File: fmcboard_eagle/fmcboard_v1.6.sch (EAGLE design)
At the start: 234 parts, among them IC1 OPA699ID, IC10 LM358, IC11 7805DT, IC12 SN74AUC2G66DCTR, IC13 SN74AUC2G66DCTR, IC14 SN74AUC2G66DCTR, IC15 SN74AUC2G66DCTR, IC16 DAC7578SPWR, IC17 SN74AUC2G66DCTR, IC18 SN74AUC2G66DCTR, IC19 SN74AUC2G66DCTR, IC2 DAC7578SPWR, IC20 SN74AUC2G66DCTR, IC21 74AUP2GU04GW, IC22 74AUP2GU04GW, IC23 74AUP2GU04GW, IC24 74AUP2GU04GW, IC25 MC7905ACD2TR4G, IC26 AMS1117-1.8, IC29 LM337KVURG3, IC3 LTC6229IMS8E#TRPBF, IC4 OPA695IDR, IC5 LTC6229IMS8E#TRPBF, IC6 OPA695IDR, IC7 OPA699ID, IC8 LM358, IC9 LM358, J1 8pin, J10 4p-2.54, J11 4p-2.54, J12 4p-2.54, J13 4p-2.54, J2 ASP-134604-01, J3 4p-2.54, J4 4p-2.54, J5 4p-2.54, J6 4p-2.54, J7 4p-2.54, J8 4p-2.54, J9 8pin, U1 TXS0108EPWR

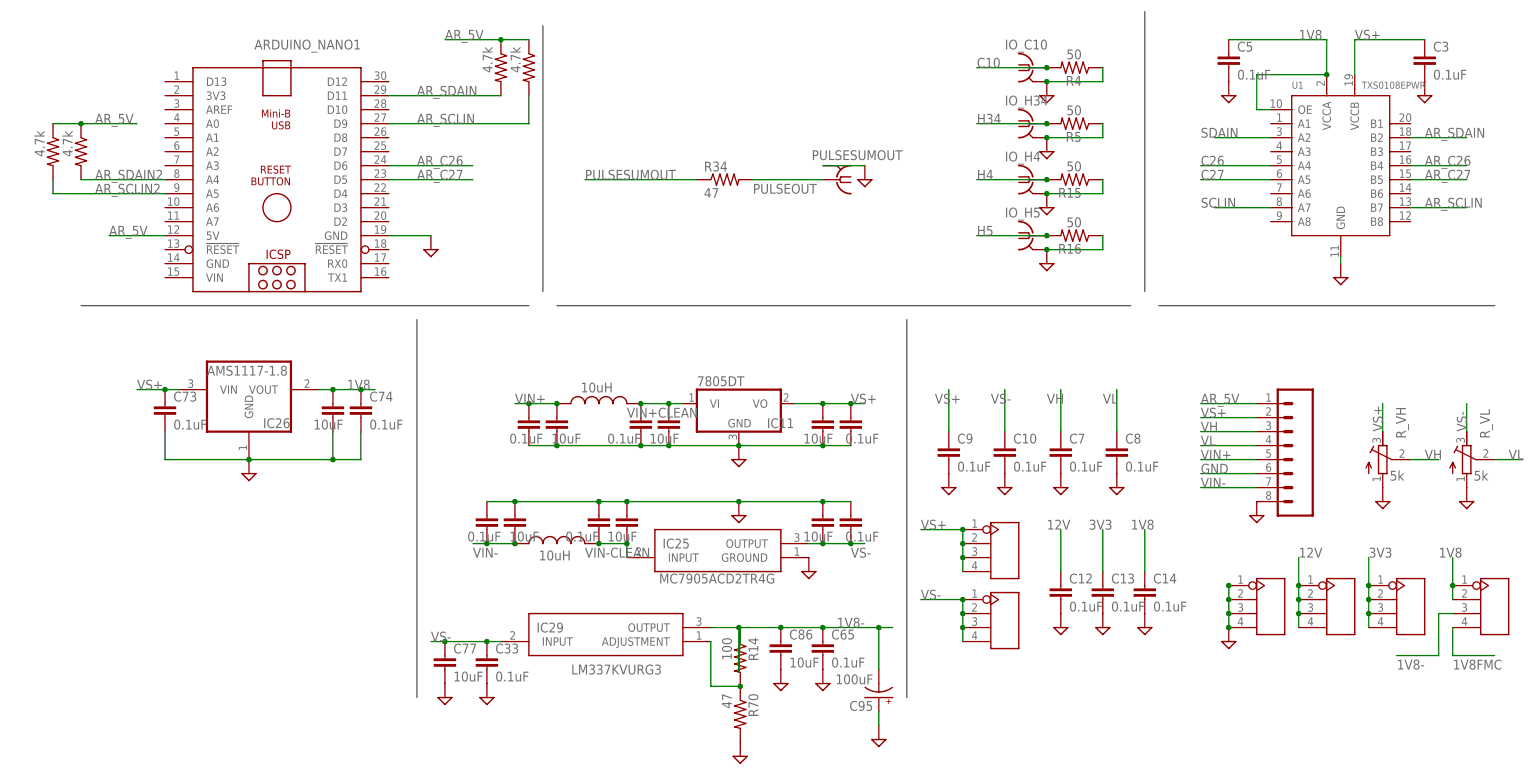
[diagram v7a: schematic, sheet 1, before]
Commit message: v1.65 C26 and C27 to A0 and A1 on arduino Remove level shifter, replace with 4.7k resistors
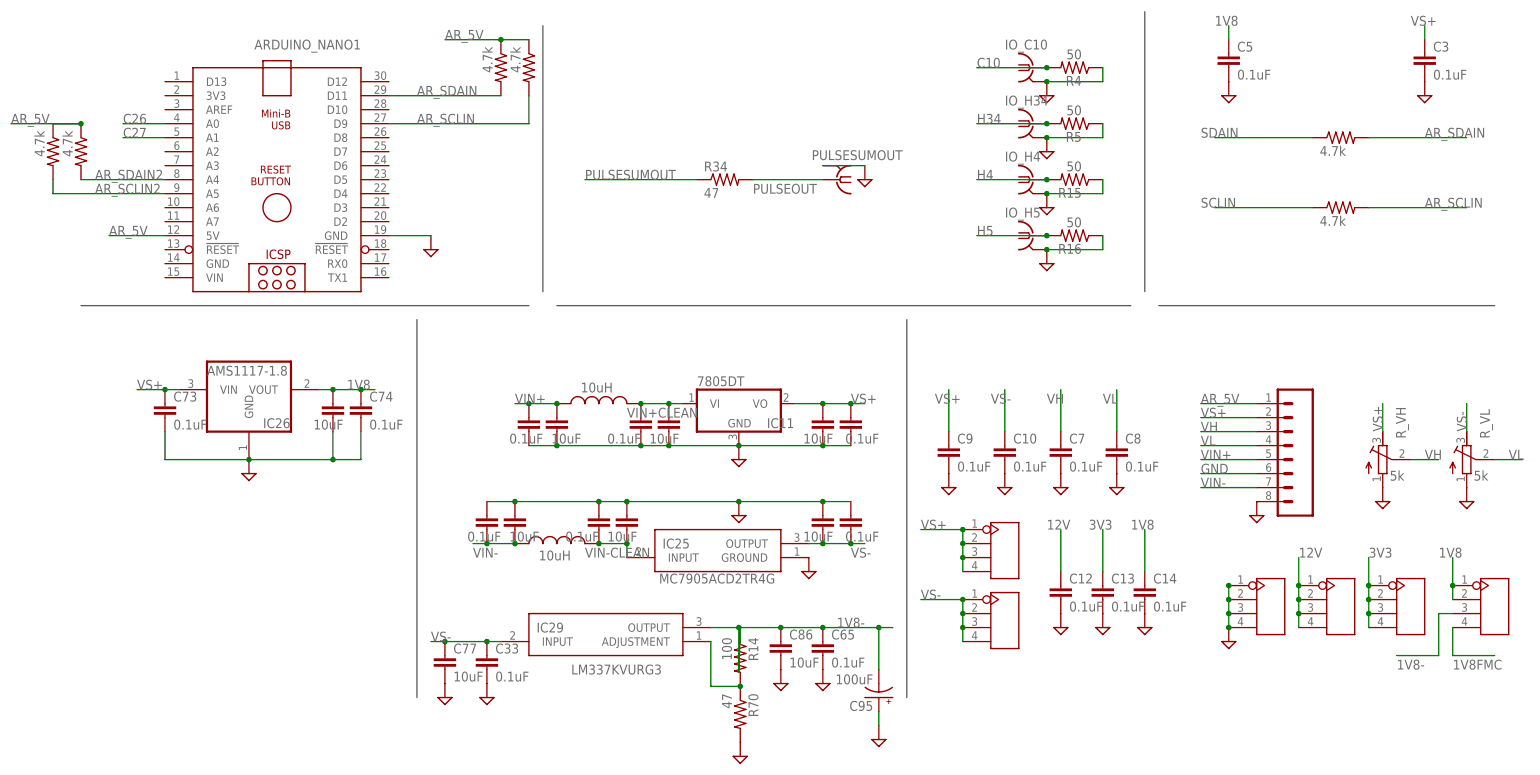
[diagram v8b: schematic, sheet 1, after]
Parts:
- removed U1: TXS0108EPWR, Seeed-IC:LOGIC-TXS0108EPWR(TSSOP20)
- added R87, R90: 4.7k, rcl:R-US_R0805
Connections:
- removed net AR_C26: ARDUINO_NANO1.D6, U1.B4
- removed net AR_C27: ARDUINO_NANO1.D5, U1.B5
- net 1V8: no longer U1.OE, U1.VCCA
- net AR_SCLIN: now also R90.2; no longer U1.B7
- net AR_SDAIN: now also R87.2; no longer U1.B2
- net C26: now also ARDUINO_NANO1.A0; no longer U1.A4
- net C27: now also ARDUINO_NANO1.A1; no longer U1.A5
- net GND: no longer U1.GND
- net SCLIN: now also R90.1; no longer U1.A7
- net SDAIN: now also R87.1; no longer U1.A2
- net VS+: no longer U1.VCCB
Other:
- note added: "Level limiter"
- note removed: "Level shifter"
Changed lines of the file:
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@@
 <part name="SUPPLY3" library="supply2" library_urn="urn:adsk.eagle:library:372" deviceset="GND" device=""/>
 <part name="SUPPLY7" library="supply2" library_urn="urn:adsk.eagle:library:372" deviceset="GND" device=""/>
-<part name="U1" library="Seeed-IC" library_urn="urn:adsk.eagle:library:470" deviceset="LOGIC-TXS0108EPWR(TSSOP20)" device="" package3d_urn="urn:adsk.eagle:package:32642/1" value="TXS0108EPWR"/>
-<part name="SUPPLY8" library="supply2" library_urn="urn:adsk.eagle:library:372" deviceset="GND" device=""/>
 <part name="C3" library="SparkFun-Passives" deviceset="CAP" device="0805" value="0.1uF"/>
 <part name="C5" library="SparkFun-Passives" deviceset="CAP" device="0805" value="0.1uF"/>
@@
 <part name="J10" library="Seeed-Connector" library_urn="urn:adsk.eagle:library:478" deviceset="DIP-BLACK-FEMALE-HEADER-VERT(4P-2.54)" device="" package3d_urn="urn:adsk.eagle:package:33137/1" value="4p-2.54"/>
 <part name="SUPPLY68" library="supply2" library_urn="urn:adsk.eagle:library:372" deviceset="GND" device=""/>
+<part name="R87" library="rcl" library_urn="urn:adsk.eagle:library:334" deviceset="R-US_" device="R0805" package3d_urn="urn:adsk.eagle:package:23553/2" value="4.7k"/>
+<part name="R90" library="rcl" library_urn="urn:adsk.eagle:library:334" deviceset="R-US_" device="R0805" package3d_urn="urn:adsk.eagle:package:23553/2" value="4.7k"/>
 </parts>
 <sheets>
@@
 <wire x1="68.58" y1="53.34" x2="68.58" y2="-15.24" width="0.1524" layer="97"/>
 <text x="7.62" y="101.6" size="1.778" layer="90">IO</text>
-<text x="116.84" y="60.96" size="1.778" layer="90">Level shifter</text>
+<text x="116.84" y="60.96" size="1.778" layer="90">Level limiter</text>
 <wire x1="-81.28" y1="55.88" x2="0" y2="55.88" width="0.1524" layer="97"/>
 <text x="-83.82" y="104.14" size="1.778" layer="90">Arduino</text>
@@
 <instance part="J4" gate="G$1" x="134.62" y="1.27" smashed="yes"/>
 <instance part="SUPPLY7" gate="GND" x="127" y="-5.08" smashed="yes"/>
-<instance part="U1" gate="G$1" x="147.32" y="81.28" smashed="yes">
-<attribute name="NAME" x="138.43" y="95.25" size="1.27" layer="95" ratio="10"/>
-<attribute name="VALUE" x="151.13" y="95.25" size="1.27" layer="96" ratio="10"/>
-</instance>
-<instance part="SUPPLY8" gate="GND" x="147.32" y="60.96" smashed="yes"/>
 <instance part="C3" gate="G$1" x="162.56" y="99.06" smashed="yes">
 <attribute name="NAME" x="164.084" y="101.981" size="1.778" layer="95"/>
@@
 </instance>
 <instance part="SUPPLY125" gate="GND" x="63.5" y="-22.86" smashed="yes"/>
+<instance part="R87" gate="G$1" x="147.32" y="86.36" smashed="yes">
+<attribute name="VALUE" x="143.51" y="83.058" size="1.778" layer="96"/>
+</instance>
+<instance part="R90" gate="G$1" x="147.32" y="73.66" smashed="yes">
+<attribute name="VALUE" x="143.51" y="70.358" size="1.778" layer="96"/>
+</instance>
 </instances>
 <busses>
@@
 <junction x="127" y="2.54"/>
 <junction x="127" y="5.08"/>
-</segment>
-<segment>
-<pinref part="U1" gate="G$1" pin="GND"/>
-<pinref part="SUPPLY8" gate="GND" pin="GND"/>
-<wire x1="147.32" y1="64.77" x2="147.32" y2="63.5" width="0.1524" layer="91"/>
 </segment>
 <segment>
@@
 <net name="1V8" class="1">
 <segment>
-<pinref part="U1" gate="G$1" pin="VCCA"/>
-<wire x1="144.78" y1="97.79" x2="144.78" y2="104.14" width="0.1524" layer="91"/>
-<label x="139.7" y="104.14" size="1.778" layer="95"/>
-<wire x1="144.78" y1="97.79" x2="132.08" y2="97.79" width="0.1524" layer="91"/>
-<wire x1="132.08" y1="97.79" x2="132.08" y2="91.44" width="0.1524" layer="91"/>
-<junction x="144.78" y="97.79"/>
-<pinref part="U1" gate="G$1" pin="OE"/>
-<wire x1="132.08" y1="91.44" x2="134.62" y2="91.44" width="0.1524" layer="91"/>
+<label x="124.46" y="106.68" size="1.778" layer="95"/>
 <pinref part="C5" gate="G$1" pin="1"/>
-<wire x1="127" y1="104.14" x2="144.78" y2="104.14" width="0.1524" layer="91"/>
+<wire x1="127" y1="104.14" x2="127" y2="106.68" width="0.1524" layer="91"/>
 </segment>
 <segment>
@@
 <net name="SDAIN" class="1">
 <segment>
-<pinref part="U1" gate="G$1" pin="A2"/>
-<wire x1="134.62" y1="86.36" x2="124.46" y2="86.36" width="0.1524" layer="91"/>
+<wire x1="142.24" y1="86.36" x2="124.46" y2="86.36" width="0.1524" layer="91"/>
 <label x="121.92" y="86.36" size="1.778" layer="95"/>
+<pinref part="R87" gate="G$1" pin="1"/>
 </segment>
 </net>
 <net name="VS+" class="1">
 <segment>
-<pinref part="U1" gate="G$1" pin="VCCB"/>
-<wire x1="149.86" y1="97.79" x2="149.86" y2="104.14" width="0.1524" layer="91"/>
-<label x="149.86" y="104.14" size="1.778" layer="95"/>
+<label x="160.02" y="106.68" size="1.778" layer="95"/>
 <pinref part="C3" gate="G$1" pin="1"/>
-<wire x1="149.86" y1="104.14" x2="162.56" y2="104.14" width="0.1524" layer="91"/>
+<wire x1="162.56" y1="106.68" x2="162.56" y2="104.14" width="0.1524" layer="91"/>
 </segment>
 <segment>
@@
 <net name="SCLIN" class="0">
 <segment>
-<pinref part="U1" gate="G$1" pin="A7"/>
-<wire x1="134.62" y1="73.66" x2="124.46" y2="73.66" width="0.1524" layer="91"/>
+<wire x1="142.24" y1="73.66" x2="124.46" y2="73.66" width="0.1524" layer="91"/>
 <label x="121.92" y="73.66" size="1.778" layer="95"/>
+<pinref part="R90" gate="G$1" pin="1"/>
 </segment>
 </net>
@@
 </segment>
 <segment>
-<pinref part="U1" gate="G$1" pin="B2"/>
-<wire x1="160.02" y1="86.36" x2="170.18" y2="86.36" width="0.1524" layer="91"/>
+<wire x1="152.4" y1="86.36" x2="170.18" y2="86.36" width="0.1524" layer="91"/>
 <label x="162.56" y="86.36" size="1.778" layer="95"/>
+<pinref part="R87" gate="G$1" pin="2"/>
 </segment>
 </net>
@@
 </segment>
 <segment>
-<pinref part="U1" gate="G$1" pin="B7"/>
-<wire x1="160.02" y1="73.66" x2="170.18" y2="73.66" width="0.1524" layer="91"/>
+<wire x1="152.4" y1="73.66" x2="170.18" y2="73.66" width="0.1524" layer="91"/>
 <label x="162.56" y="73.66" size="1.778" layer="95"/>
+<pinref part="R90" gate="G$1" pin="2"/>
 </segment>
 </net>
@@
 </segment>
 </net>
-<net name="C26" class="0">
-<segment>
-<pinref part="U1" gate="G$1" pin="A4"/>
-<wire x1="121.92" y1="81.28" x2="134.62" y2="81.28" width="0.1524" layer="91"/>
-<label x="121.92" y="81.28" size="1.778" layer="95"/>
-</segment>
-</net>
-<net name="C27" class="0">
-<segment>
-<pinref part="U1" gate="G$1" pin="A5"/>
-<wire x1="121.92" y1="78.74" x2="134.62" y2="78.74" width="0.1524" layer="91"/>
-<label x="121.92" y="78.74" size="1.778" layer="95"/>
-</segment>
-</net>
-<net name="AR_C26" class="0">
-<segment>
-<pinref part="ARDUINO_NANO1" gate="G$1" pin="D6"/>
-<wire x1="-25.4" y1="81.28" x2="-10.16" y2="81.28" width="0.1524" layer="91"/>
-<label x="-20.32" y="81.28" size="1.778" layer="95"/>
-</segment>
-<segment>
-<pinref part="U1" gate="G$1" pin="B4"/>
-<wire x1="170.18" y1="81.28" x2="160.02" y2="81.28" width="0.1524" layer="91"/>
-<label x="162.56" y="81.28" size="1.778" layer="95"/>
-</segment>
-</net>
 <net name="PULSESUMOUT" class="0">
 <segment>
@@
 <pinref part="R48" gate="G$1" pin="1"/>
 <wire x1="-86.36" y1="88.9" x2="-81.28" y2="88.9" width="0.1524" layer="91"/>
-<wire x1="-81.28" y1="88.9" x2="-71.12" y2="88.9" width="0.1524" layer="91"/>
+<wire x1="-81.28" y1="88.9" x2="-93.98" y2="88.9" width="0.1524" layer="91"/>
 <junction x="-81.28" y="88.9"/>
-<label x="-78.74" y="88.9" size="1.778" layer="95"/>
+<label x="-93.98" y="88.9" size="1.778" layer="95"/>
 </segment>
 <segment>
@@
 </segment>
 </net>
-<net name="AR_C27" class="0">
-<segment>
-<pinref part="U1" gate="G$1" pin="B5"/>
-<wire x1="160.02" y1="78.74" x2="170.18" y2="78.74" width="0.1524" layer="91"/>
-<label x="162.56" y="78.74" size="1.778" layer="95"/>
-</segment>
-<segment>
-<pinref part="ARDUINO_NANO1" gate="G$1" pin="D5"/>
-<wire x1="-25.4" y1="78.74" x2="-10.16" y2="78.74" width="0.1524" layer="91"/>
-<label x="-20.32" y="78.74" size="1.778" layer="95"/>
-</segment>
-</net>
+<net name="C26" class="0">
+<segment>
+<pinref part="ARDUINO_NANO1" gate="G$1" pin="A0"/>
+<wire x1="-66.04" y1="88.9" x2="-73.66" y2="88.9" width="0.1524" layer="91"/>
+<label x="-73.66" y="88.9" size="1.778" layer="95"/>
+</segment>
+</net>
+<net name="C27" class="0">
+<segment>
+<pinref part="ARDUINO_NANO1" gate="G$1" pin="A1"/>
+<wire x1="-66.04" y1="86.36" x2="-73.66" y2="86.36" width="0.1524" layer="91"/>
+<label x="-73.66" y="86.36" size="1.778" layer="95"/>
+</segment>
+</net>
